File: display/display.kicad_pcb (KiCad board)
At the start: 2 copper layers, 35.8 x 14 mm, 19 parts, among them P1 51281-1694, P2 CONN_14

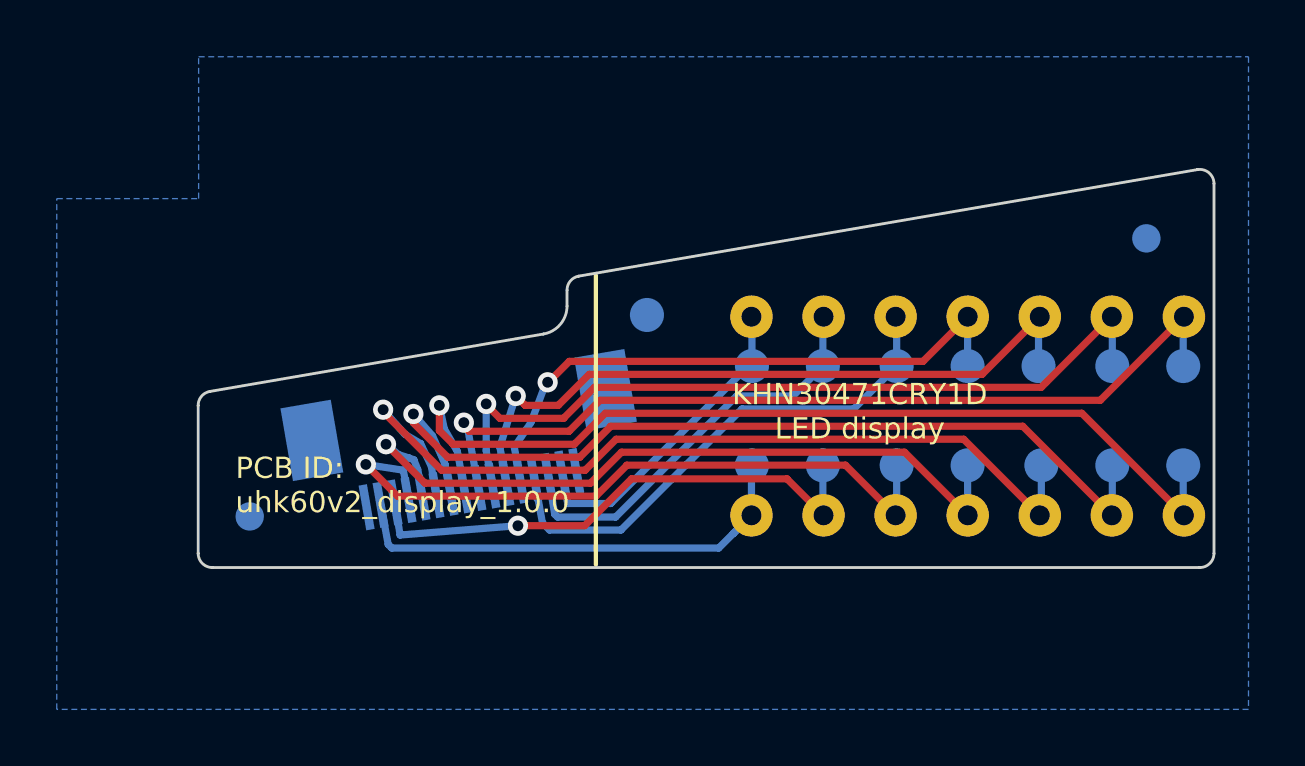
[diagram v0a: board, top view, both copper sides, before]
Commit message: Improve silk screen.
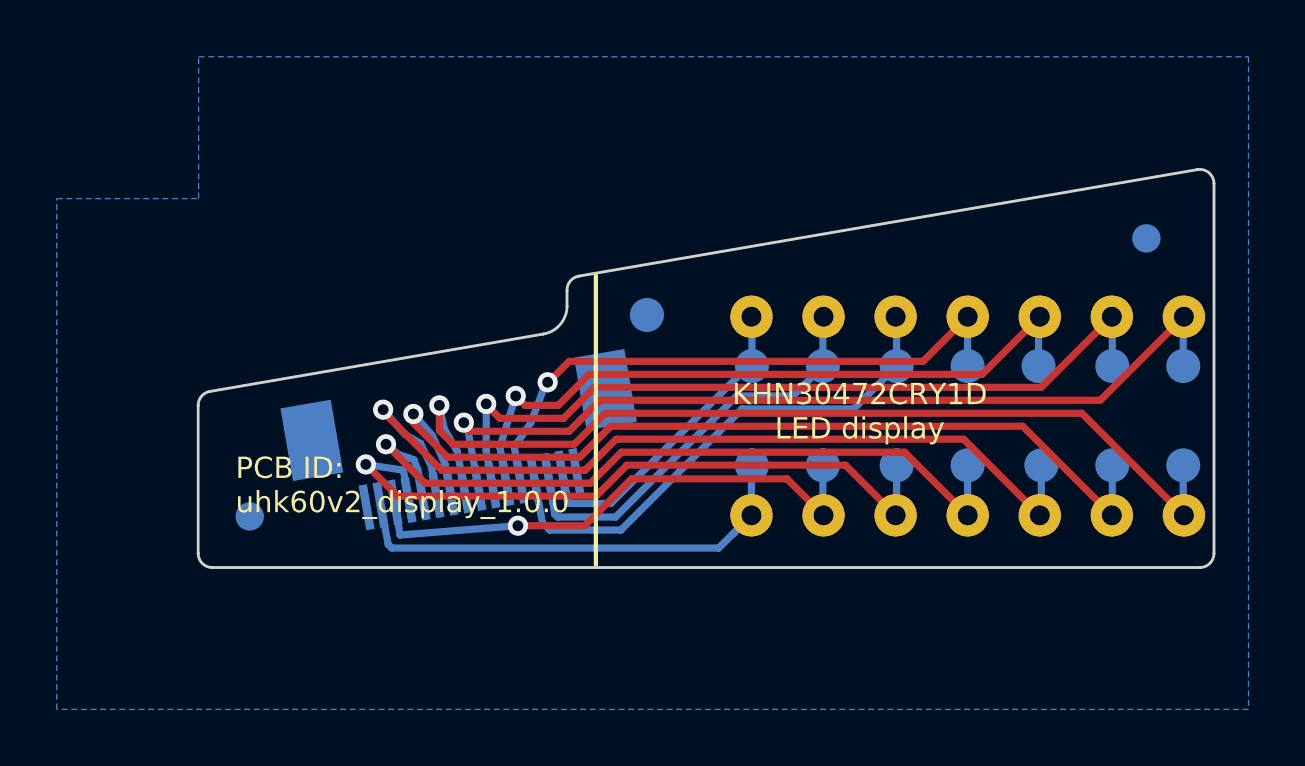
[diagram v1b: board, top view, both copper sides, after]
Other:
- board text added: "KHN30472CRY1D LED display"
- board text removed: "KHN30471CRY1D LED display"
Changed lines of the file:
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@@
-(kicad_pcb (version 20171130) (host pcbnew "(5.0.0)")
+(kicad_pcb (version 20171130) (host pcbnew 5.0.2-bee76a0~70~ubuntu18.04.1)
   (general
     (thickness 1.6002)
@@
   (page A4)
   (title_block
-    (title "UHK60v2 - LED Display Board")
-    (rev 1.0.0)
+    (title "UHK 60 v2 - LED Display Board")
+    (rev 2.0.0)
     (company "Ultimate Gadget Laboratories Kft.")
   )
@@
     (pad_drill 0)
     (pad_to_mask_clearance 0)
+    (solder_mask_min_width 0.25)
     (aux_axis_origin 121.875 109.075)
     (grid_origin 121.875 109.075)
@@
     )
     (fp_text value CS1 (at 0 -1.3) (layer B.SilkS)
-      (effects (font (size 0.75 0.75) (thickness 0.15)) (justify mirror))
+      (effects (font (size 0.6 0.6) (thickness 0.12)) (justify mirror))
     )
     (pad 1 smd circle (at 0 0) (size 1.2 1.2) (layers B.Cu B.Mask)
@@
     )
     (fp_text value CS2 (at 0 1.2) (layer B.SilkS)
-      (effects (font (size 0.75 0.75) (thickness 0.15)) (justify mirror))
+      (effects (font (size 0.6 0.6) (thickness 0.12)) (justify mirror))
     )
     (pad 1 smd circle (at 0 0) (size 1.2 1.2) (layers B.Cu B.Mask)
@@
     )
     (fp_text value CS3 (at 0 1.2) (layer B.SilkS)
-      (effects (font (size 0.75 0.75) (thickness 0.15)) (justify mirror))
+      (effects (font (size 0.6 0.6) (thickness 0.12)) (justify mirror))
     )
     (pad 1 smd circle (at 0 0) (size 1.2 1.2) (layers B.Cu B.Mask)
@@
     )
     (fp_text value CS4 (at 0 1.2) (layer B.SilkS)
-      (effects (font (size 0.75 0.75) (thickness 0.15)) (justify mirror))
+      (effects (font (size 0.6 0.6) (thickness 0.12)) (justify mirror))
     )
     (pad 1 smd circle (at 0 0) (size 1.2 1.2) (layers B.Cu B.Mask)
@@
     )
     (fp_text value CS5 (at 0 1.2) (layer B.SilkS)
-      (effects (font (size 0.75 0.75) (thickness 0.15)) (justify mirror))
+      (effects (font (size 0.6 0.6) (thickness 0.12)) (justify mirror))
     )
     (pad 1 smd circle (at 0 0) (size 1.2 1.2) (layers B.Cu B.Mask)
@@
     )
     (fp_text value CS6 (at 0 1.2) (layer B.SilkS)
-      (effects (font (size 0.75 0.75) (thickness 0.15)) (justify mirror))
+      (effects (font (size 0.6 0.6) (thickness 0.12)) (justify mirror))
     )
     (pad 1 smd circle (at 0 0) (size 1.2 1.2) (layers B.Cu B.Mask)
@@
     )
     (fp_text value CS7 (at 0 1.2) (layer B.SilkS)
-      (effects (font (size 0.75 0.75) (thickness 0.15)) (justify mirror))
+      (effects (font (size 0.6 0.6) (thickness 0.12)) (justify mirror))
     )
     (pad 1 smd circle (at 0 0) (size 1.2 1.2) (layers B.Cu B.Mask)
@@
     )
     (fp_text value CS8 (at 0.1 1.2) (layer B.SilkS)
-      (effects (font (size 0.75 0.75) (thickness 0.15)) (justify mirror))
+      (effects (font (size 0.6 0.6) (thickness 0.12)) (justify mirror))
     )
     (pad 1 smd circle (at 0 0) (size 1.2 1.2) (layers B.Cu B.Mask)
@@
     )
     (fp_text value SW7 (at 0 -1.3) (layer B.SilkS)
-      (effects (font (size 0.75 0.75) (thickness 0.15)) (justify mirror))
+      (effects (font (size 0.6 0.6) (thickness 0.12)) (justify mirror))
     )
     (pad 1 smd circle (at 0 0) (size 1.2 1.2) (layers B.Cu B.Mask)
@@
     )
     (fp_text value SW8 (at 0 -1.3) (layer B.SilkS)
-      (effects (font (size 0.75 0.75) (thickness 0.15)) (justify mirror))
+      (effects (font (size 0.6 0.6) (thickness 0.12)) (justify mirror))
     )
     (pad 1 smd circle (at 0 0) (size 1.2 1.2) (layers B.Cu B.Mask)
@@
     )
     (fp_text value SW9 (at 0 -1.3) (layer B.SilkS)
-      (effects (font (size 0.75 0.75) (thickness 0.15)) (justify mirror))
+      (effects (font (size 0.6 0.6) (thickness 0.12)) (justify mirror))
     )
     (pad 1 smd circle (at 0 0) (size 1.2 1.2) (layers B.Cu B.Mask)
@@
     )
     (fp_text value SW10 (at 0 -1.3) (layer B.SilkS)
-      (effects (font (size 0.75 0.75) (thickness 0.15)) (justify mirror))
+      (effects (font (size 0.6 0.6) (thickness 0.12)) (justify mirror))
     )
     (pad 1 smd circle (at 0 0) (size 1.2 1.2) (layers B.Cu B.Mask)
@@
     )
     (fp_text value SW11 (at 0 -1.3) (layer B.SilkS)
-      (effects (font (size 0.75 0.75) (thickness 0.15)) (justify mirror))
+      (effects (font (size 0.6 0.6) (thickness 0.12)) (justify mirror))
     )
     (pad 1 smd circle (at 0 0) (size 1.2 1.2) (layers B.Cu B.Mask)
@@
     )
     (fp_text value SW12 (at 0 -1.3) (layer B.SilkS)
-      (effects (font (size 0.75 0.75) (thickness 0.15)) (justify mirror))
+      (effects (font (size 0.6 0.6) (thickness 0.12)) (justify mirror))
     )
     (pad 1 smd circle (at 0 0) (size 1.2 1.2) (layers B.Cu B.Mask)
@@
     (effects (font (size 0.75 0.75) (thickness 0.15)) (justify left))
   )
-  (gr_text "KHN30471CRY1D\nLED display" (at 145.175 103.575) (layer F.SilkS)
+  (gr_text "KHN30472CRY1D\nLED display" (at 145.175 103.575) (layer F.SilkS)
     (effects (font (size 0.75 0.75) (thickness 0.15)))
   )

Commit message: Update pogo pin footprints and improve silk screen.
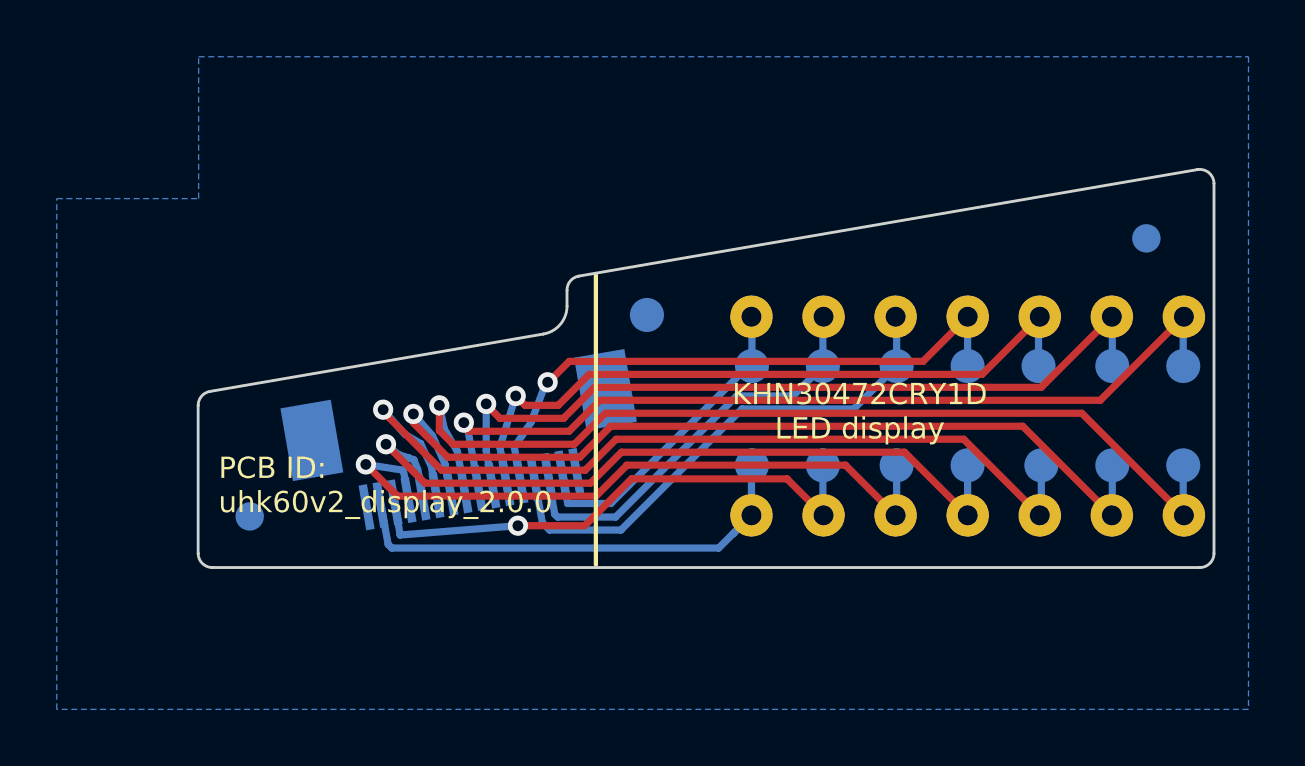
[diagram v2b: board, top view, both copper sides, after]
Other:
- board text added: "PCB ID: uhk60v2_display_2.0.0"
- board text removed: "PCB ID: uhk60v2_display_1.0.0"
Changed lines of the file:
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@@
   (gr_line (start 135.27385 98.805944) (end 157.073845 95.052999) (angle 90) (layer Edge.Cuts) (width 0.1))
   (gr_arc (start 122.358734 108.576078) (end 121.858673 108.576147) (angle -89.94233769) (layer Edge.Cuts) (width 0.1))
-  (gr_text "PCB ID:\nuhk60v2_display_1.0.0" (at 123.175 106.175) (layer F.SilkS)
+  (gr_text "PCB ID:\nuhk60v2_display_2.0.0" (at 122.575 106.175) (layer F.SilkS)
     (effects (font (size 0.75 0.75) (thickness 0.15)) (justify left))
   )
